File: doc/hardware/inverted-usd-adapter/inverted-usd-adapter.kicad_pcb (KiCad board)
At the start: 2 copper layers, 17 x 35 mm, 2 parts, among them J1 usd-plug, P1 CONN_02X04

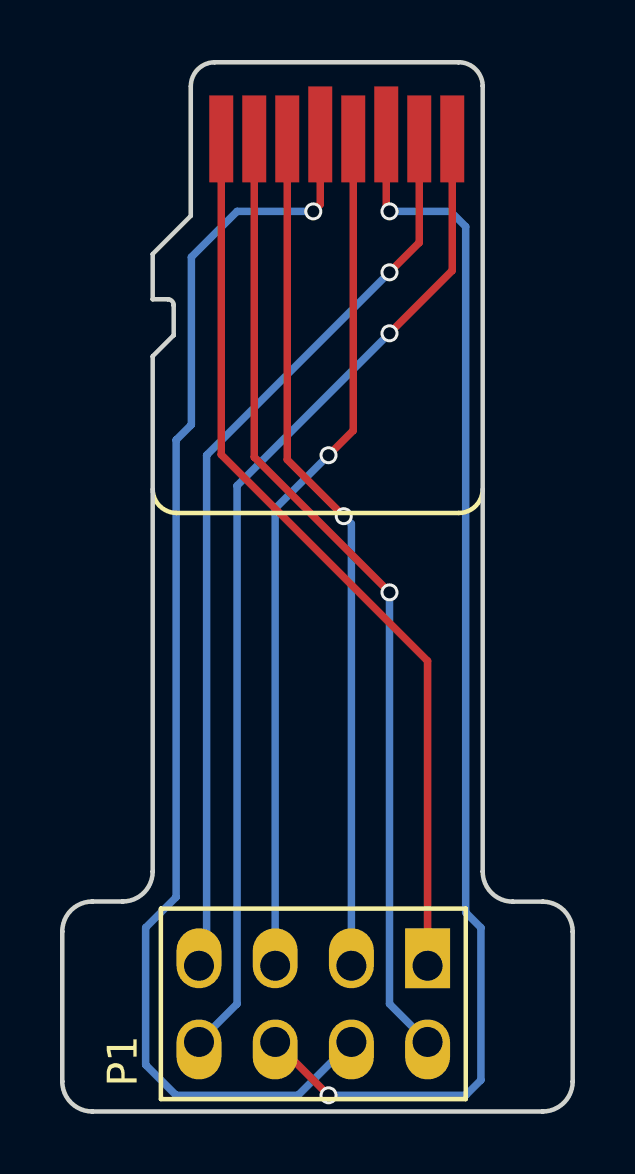
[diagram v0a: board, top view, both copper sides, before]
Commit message: Fix IDC connector on usd-adapter and add inverted version of it
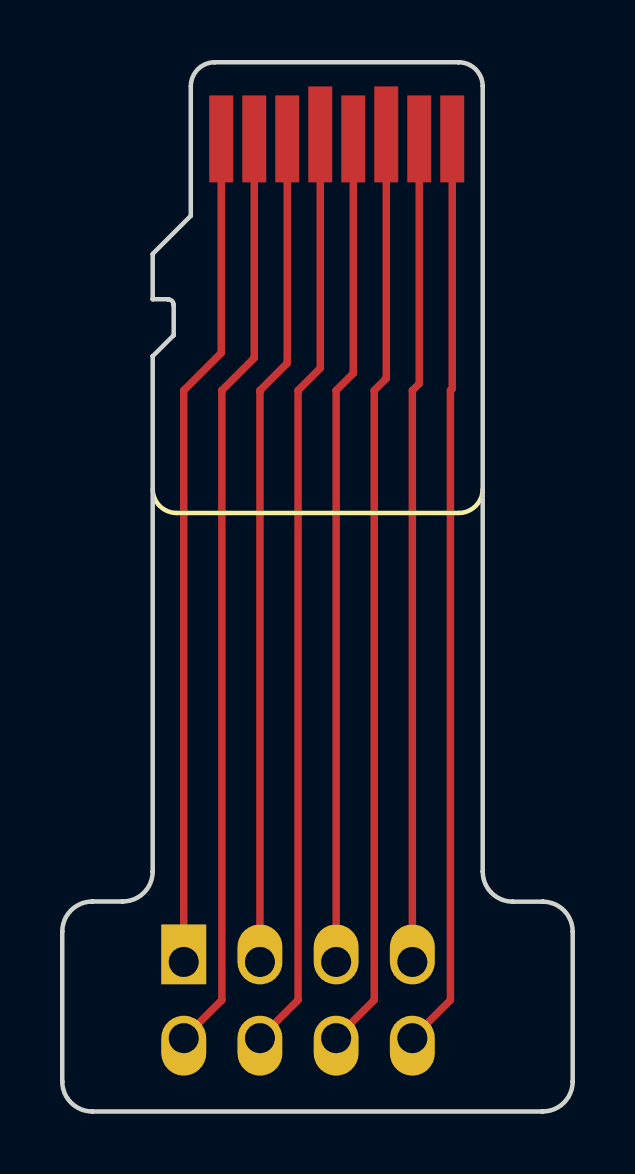
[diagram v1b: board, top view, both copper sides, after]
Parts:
- P1: moved to B.Cu
- moved P1 0.52 mm to (149.9, 121.3), turned to 0 degrees
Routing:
- net /N4: track 42.9 -> 31.0 mm, vias 1 -> 0
- net /N6: track 41.8 -> 30.8 mm, vias 2 -> 0
- net /N7: track 30.6 -> 27.5 mm, vias 1 -> 0
- net /N8: track 33.6 -> 30.5 mm, vias 1 -> 0
- net /N1: track 30.4 -> 28.0 mm
- net /N2: track 32.5 -> 30.9 mm, vias 1 -> 0
- net /N5: track 28.6 -> 27.7 mm, vias 1 -> 0
- net /N3: track 28.4 -> 27.8 mm, vias 1 -> 0
